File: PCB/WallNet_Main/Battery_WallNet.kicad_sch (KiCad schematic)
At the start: 21 parts, among them J2 USB_C_Receptacle_PowerOnly_6P, J3 Conn_01x04_Pin, U3 BQ25895RTWT

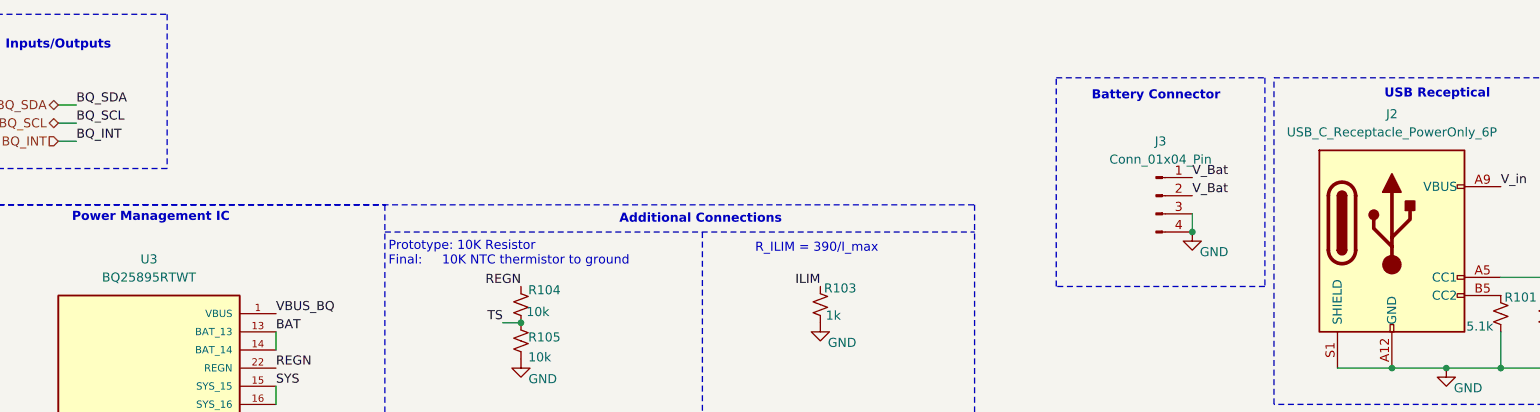
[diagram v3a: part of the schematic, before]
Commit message: Parts complete for schematic
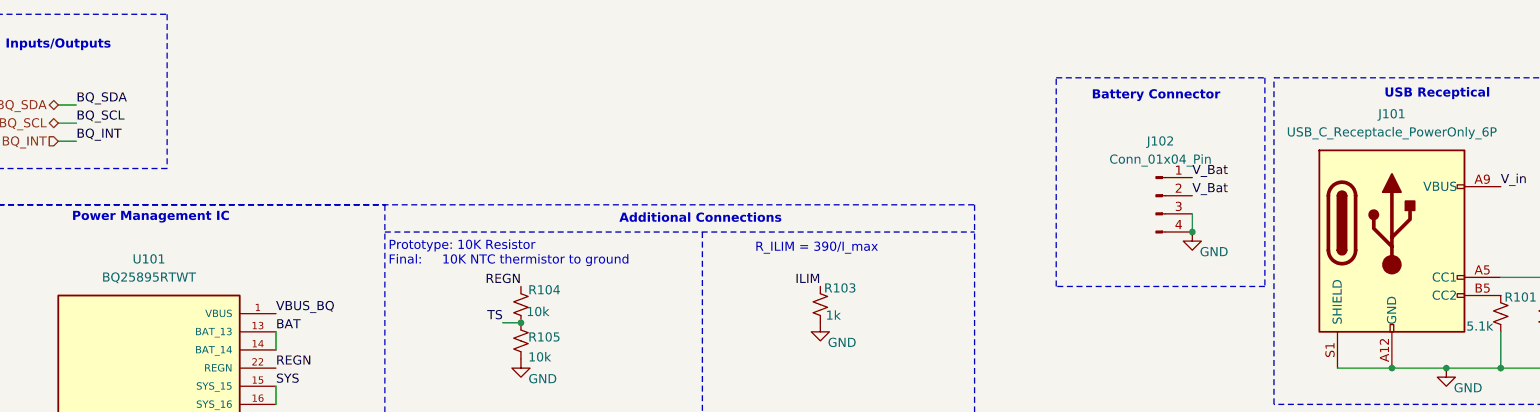
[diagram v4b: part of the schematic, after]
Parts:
- C101, C104, C105, C106, C107: footprint (none) -> Capacitor_SMD:C_0201_0603Metric
- C102, C103: footprint (none) -> Capacitor_SMD:C_0805_2012Metric
- J101: renamed from J2; footprint (none) -> Connector_USB:USB_C_Receptacle_GCT_USB4125-xx-x-0190_6P_TopMnt_Horizontal
- R101, R102, R103, R104, R105, R106, R107, R108, R11: footprint (none) -> Resistor_SMD:R_0201_0603Metric
- renumbered J3 to J102, U3 to U101
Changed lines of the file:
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@@
 			)
 		)
-		(property "Footprint" ""
+		(property "Footprint" "Resistor_SMD:R_0201_0603Metric"
 			(at 119.38 82.55 0)
 			(effects
@@
 		(dnp no)
 		(fields_autoplaced yes)
-		(property "Reference" "J2"
+		(property "Reference" "J101"
 			(at 227.33 27.94 0)
 			(effects
@@
 			)
 		)
-		(property "Footprint" ""
+		(property "Footprint" "Connector_USB:USB_C_Receptacle_GCT_USB4125-xx-x-0190_6P_TopMnt_Horizontal"
 			(at 231.14 43.18 0)
 			(effects
@@
 			(project "WallNet_Main"
 				(path "/3272dd14-9e34-4275-b10b-c06dab1b3ca1/ac25aec4-60b5-4d7f-9f99-a074eef21076"
-					(reference "J2")
+					(reference "J101")
 					(unit 1)
 				)
@@
 			)
 		)
-		(property "Footprint" ""
+		(property "Footprint" "Resistor_SMD:R_0201_0603Metric"
 			(at 248.92 55.88 0)
 			(effects
@@
 			)
 		)
-		(property "Footprint" ""
+		(property "Footprint" "Capacitor_SMD:C_0201_0603Metric"
 			(at 105.41 77.47 0)
 			(effects
@@
 			)
 		)
-		(property "Footprint" ""
+		(property "Footprint" "Capacitor_SMD:C_0201_0603Metric"
 			(at 105.41 121.92 0)
 			(effects
@@
 			)
 		)
-		(property "Footprint" ""
+		(property "Footprint" "Capacitor_SMD:C_0201_0603Metric"
 			(at 123.19 121.92 0)
 			(effects
@@
 		(dnp no)
 		(fields_autoplaced yes)
-		(property "Reference" "U3"
+		(property "Reference" "U101"
 			(at 53.34 48.26 0)
 			(effects
@@
 			(project "WallNet_Main"
 				(path "/3272dd14-9e34-4275-b10b-c06dab1b3ca1/ac25aec4-60b5-4d7f-9f99-a074eef21076"
-					(reference "U3")
+					(reference "U101")
 					(unit 1)
 				)
@@
 			)
 		)
-		(property "Footprint" ""
+		(property "Footprint" "Capacitor_SMD:C_0201_0603Metric"
 			(at 132.08 121.92 0)
 			(effects
@@
 			)
 		)
-		(property "Footprint" ""
+		(property "Footprint" "Resistor_SMD:R_0201_0603Metric"
 			(at 105.41 54.61 0)
 			(effects
@@
 			)
 		)
-		(property "Footprint" ""
+		(property "Footprint" "Resistor_SMD:R_0201_0603Metric"
 			(at 143.51 93.98 0)
 			(effects
@@
 			)
 		)
-		(property "Footprint" ""
+		(property "Footprint" "Resistor_SMD:R_0201_0603Metric"
 			(at 157.48 99.06 0)
 			(effects
@@
 			)
 		)
-		(property "Footprint" ""
+		(property "Footprint" "Capacitor_SMD:C_0201_0603Metric"
 			(at 158.75 77.47 0)
 			(effects
@@
 			)
 		)
-		(property "Footprint" ""
+		(property "Footprint" "Resistor_SMD:R_0201_0603Metric"
 			(at 147.32 54.61 0)
 			(effects
@@
 			)
 		)
-		(property "Footprint" ""
+		(property "Footprint" "Resistor_SMD:R_0201_0603Metric"
 			(at 151.13 96.52 0)
 			(effects
@@
 			)
 		)
-		(property "Footprint" ""
+		(property "Footprint" "Resistor_SMD:R_0201_0603Metric"
 			(at 242.57 55.88 0)
 			(effects
@@
 			)
 		)
-		(property "Footprint" ""
+		(property "Footprint" "Resistor_SMD:R_0201_0603Metric"
 			(at 105.41 59.69 0)
 			(effects
@@
 			)
 		)
-		(property "Footprint" ""
+		(property "Footprint" "Capacitor_SMD:C_0805_2012Metric"
 			(at 93.98 77.47 0)
 			(effects
@@
 			)
 		)
-		(property "Footprint" ""
+		(property "Footprint" "Capacitor_SMD:C_0805_2012Metric"
 			(at 137.16 77.47 0)
 			(effects
@@
 		(dnp no)
 		(fields_autoplaced yes)
-		(property "Reference" "J3"
+		(property "Reference" "J102"
 			(at 194.945 31.75 0)
 			(effects
@@
 			(project "WallNet_Main"
 				(path "/3272dd14-9e34-4275-b10b-c06dab1b3ca1/ac25aec4-60b5-4d7f-9f99-a074eef21076"
-					(reference "J3")
-					(unit 1)
-				)
+					(reference "J102")
+					(unit 1)
+				)

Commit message: Schematic done, updated layout
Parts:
- C101, C104, C105, C106, C107: footprint Capacitor_SMD:C_0201_0603Metric -> Capacitor_SMD:C_0603_1608Metric
- D101: footprint (none) -> Diode_SMD:D_0603_1608Metric
- J102: footprint Connector_Molex:Molex_CLIK-Mate_502494-0470_1x04-1MP_P2.00mm_Horizontal -> Connector_Molex:Molex_PicoBlade_53261-0471_1x04-1MP_P1.25mm_Horizontal
- R101, R102, R103, R104, R105, R106, R107, R108: footprint Resistor_SMD:R_0201_0603Metric -> Resistor_SMD:R_0603_1608Metric
- R109: renamed from R11; footprint Resistor_SMD:R_0201_0603Metric -> Resistor_SMD:R_0603_1608Metric
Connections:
- net VDD_nRF is gone; now on net VDD_nrf: D101.2 (A), R106.1, R107.1, R108.1
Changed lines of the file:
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@@
 	(wire
 		(pts
+			(xy 119.38 73.66) (xy 119.38 74.93)
+		)
+		(stroke
+			(width 0)
+			(type default)
+		)
+	)
+	(wire
+		(pts
 			(xy 40.64 31.75) (xy 43.18 31.75)
 		)
@@
 		)
 	)
-	(label "VDD_nRF"
-		(at 146.05 91.44 180)
-		(effects
-			(font
-				(size 1.27 1.27)
-			)
-			(justify right bottom)
-		)
-	)
 	(label "BTST"
 		(at 71.12 81.28 0)
@@
 		)
 	)
-	(label "VDD_nRF"
-		(at 119.38 74.93 180)
-		(effects
-			(font
-				(size 1.27 1.27)
-			)
-			(justify right bottom)
-		)
-	)
 	(label "CE"
 		(at 113.03 95.25 180)
@@
 	)
 	(global_label "VDD_nrf"
+		(shape input)
+		(at 119.38 73.66 180)
+		(fields_autoplaced yes)
+		(effects
+			(font
+				(size 1.27 1.27)
+			)
+			(justify right)
+		)
+		(property "Intersheetrefs" "${INTERSHEET_REFS}"
+			(at 109.1377 73.66 0)
+			(effects
+				(font
+					(size 1.27 1.27)
+				)
+				(justify right)
+				(hide yes)
+			)
+		)
+	)
+	(global_label "VDD_nrf"
 		(shape output)
 		(at 142.24 119.38 0)
@@
 		)
 	)
+	(global_label "VDD_nrf"
+		(shape input)
+		(at 143.51 91.44 180)
+		(fields_autoplaced yes)
+		(effects
+			(font
+				(size 1.27 1.27)
+			)
+			(justify right)
+		)
+		(property "Intersheetrefs" "${INTERSHEET_REFS}"
+			(at 133.2677 91.44 0)
+			(effects
+				(font
+					(size 1.27 1.27)
+				)
+				(justify right)
+				(hide yes)
+			)
+		)
+	)
 	(hierarchical_label "BQ_INT"
 		(shape input)
@@
 		(on_board yes)
 		(dnp no)
-		(property "Reference" "R11"
+		(property "Reference" "R109"
 			(at 120.396 81.28 0)
 			(effects
@@
 			)
 		)
-		(property "Footprint" "Resistor_SMD:R_0201_0603Metric"
+		(property "Footprint" "Resistor_SMD:R_0603_1608Metric"
 			(at 119.38 82.55 0)
 			(effects
@@
 			(project "WallNet_Main"
 				(path "/3272dd14-9e34-4275-b10b-c06dab1b3ca1/ac25aec4-60b5-4d7f-9f99-a074eef21076"
-					(reference "R11")
+					(reference "R109")
 					(unit 1)
 				)
@@
 			)
 		)
-		(property "Footprint" "Resistor_SMD:R_0201_0603Metric"
+		(property "Footprint" "Resistor_SMD:R_0603_1608Metric"
 			(at 248.92 55.88 0)
 			(effects
@@
 			)
 		)
-		(property "Footprint" "Capacitor_SMD:C_0201_0603Metric"
+		(property "Footprint" "Capacitor_SMD:C_0603_1608Metric"
 			(at 105.41 77.47 0)
 			(effects
@@
 			)
 		)
-		(property "Footprint" "Capacitor_SMD:C_0201_0603Metric"
+		(property "Footprint" "Capacitor_SMD:C_0603_1608Metric"
 			(at 105.41 121.92 0)
 			(effects
@@
 			)
 		)
-		(property "Footprint" "Capacitor_SMD:C_0201_0603Metric"
+		(property "Footprint" "Capacitor_SMD:C_0603_1608Metric"
 			(at 123.19 121.92 0)
 			(effects
@@
 			)
 		)
-		(property "Footprint" "Capacitor_SMD:C_0201_0603Metric"
+		(property "Footprint" "Capacitor_SMD:C_0603_1608Metric"
 			(at 132.08 121.92 0)
 			(effects
@@
 			)
 		)
-		(property "Footprint" "Resistor_SMD:R_0201_0603Metric"
+		(property "Footprint" "Resistor_SMD:R_0603_1608Metric"
 			(at 105.41 54.61 0)
 			(effects
@@
 			)
 		)
-		(property "Footprint" "Resistor_SMD:R_0201_0603Metric"
+		(property "Footprint" "Resistor_SMD:R_0603_1608Metric"
 			(at 143.51 93.98 0)
 			(effects
@@
 			)
 		)
-		(property "Footprint" "Resistor_SMD:R_0201_0603Metric"
+		(property "Footprint" "Resistor_SMD:R_0603_1608Metric"
 			(at 157.48 99.06 0)
 			(effects
@@
 			)
 		)
-		(property "Footprint" "Capacitor_SMD:C_0201_0603Metric"
+		(property "Footprint" "Capacitor_SMD:C_0603_1608Metric"
 			(at 158.75 77.47 0)
 			(effects
@@
 			)
 		)
-		(property "Footprint" "Resistor_SMD:R_0201_0603Metric"
+		(property "Footprint" "Resistor_SMD:R_0603_1608Metric"
 			(at 147.32 54.61 0)
 			(effects
@@
 			)
 		)
-		(property "Footprint" ""
+		(property "Footprint" "Diode_SMD:D_0603_1608Metric"
 			(at 119.38 77.47 90)
 			(effects
@@
 			)
 		)
-		(property "Footprint" "Resistor_SMD:R_0201_0603Metric"
+		(property "Footprint" "Resistor_SMD:R_0603_1608Metric"
 			(at 151.13 96.52 0)
 			(effects
@@
 			)
 		)
-		(property "Footprint" "Resistor_SMD:R_0201_0603Metric"
+		(property "Footprint" "Resistor_SMD:R_0603_1608Metric"
 			(at 242.57 55.88 0)
 			(effects
@@
 			)
 		)
-		(property "Footprint" "Resistor_SMD:R_0201_0603Metric"
+		(property "Footprint" "Resistor_SMD:R_0603_1608Metric"
 			(at 105.41 59.69 0)
 			(effects
@@
 			)
 		)
-		(property "Footprint" "Connector_Molex:Molex_CLIK-Mate_502494-0470_1x04-1MP_P2.00mm_Horizontal"
+		(property "Footprint" "Connector_Molex:Molex_PicoBlade_53261-0471_1x04-1MP_P1.25mm_Horizontal"
 			(at 194.31 39.37 0)
 			(effects

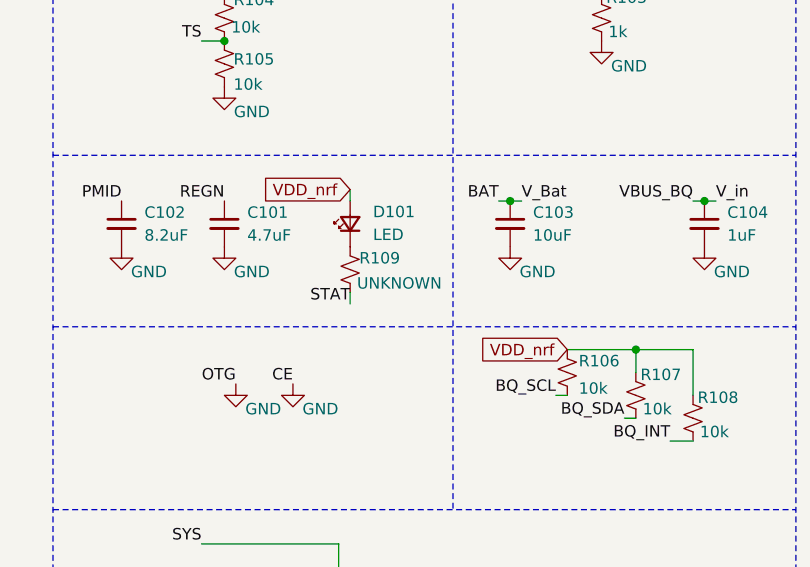
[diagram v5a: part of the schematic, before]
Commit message: added debug LED
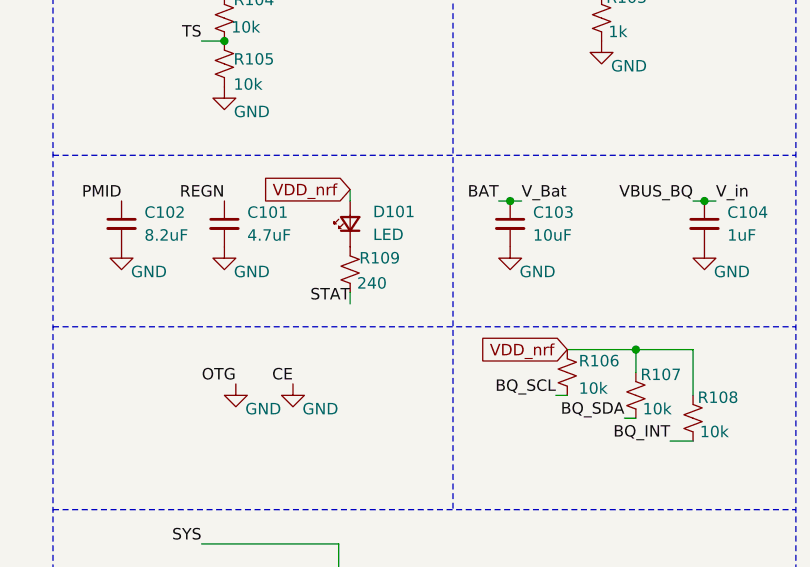
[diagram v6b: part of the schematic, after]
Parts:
- R109: value UNKNOWN -> 240
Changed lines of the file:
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@@
 			)
 		)
-		(property "Value" "UNKNOWN"
+		(property "Value" "240"
 			(at 120.142 84.074 0)
 			(effects

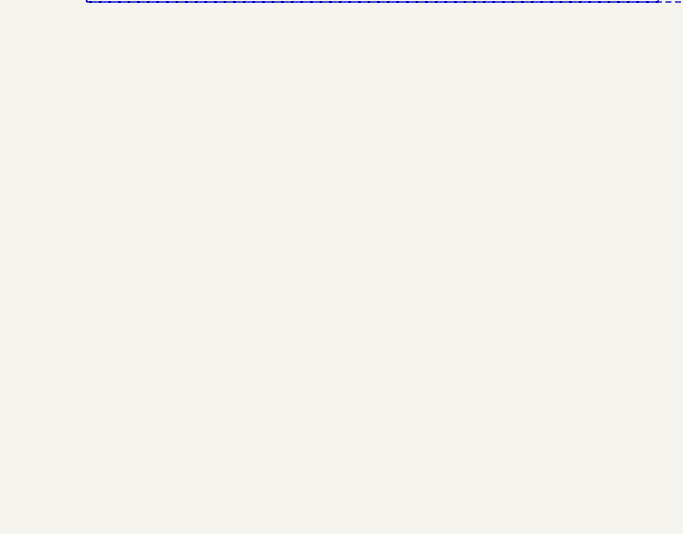
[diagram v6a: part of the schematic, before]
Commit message: "added test point debugging and mounting holes"
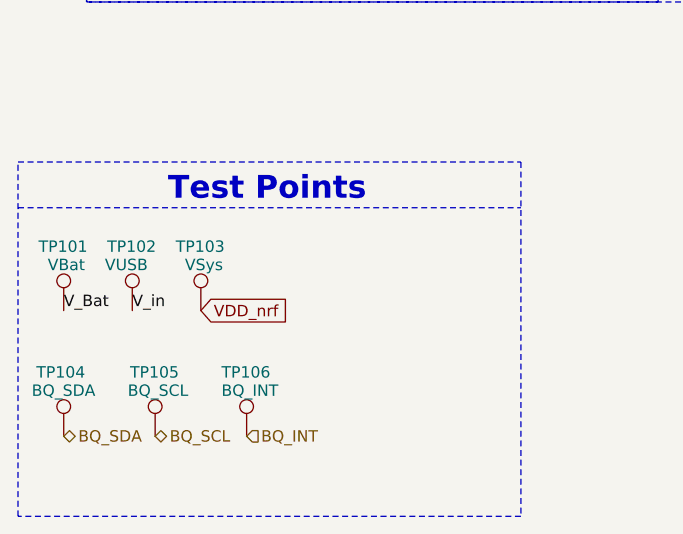
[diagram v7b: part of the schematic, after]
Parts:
- added TP101: VBat, TestPoint:TestPoint_Pad_D1.0mm, symbol Connector:TestPoint
- added TP102: VUSB, TestPoint:TestPoint_Pad_D1.0mm, symbol Connector:TestPoint
- added TP103: VSys, TestPoint:TestPoint_Pad_D1.0mm, symbol Connector:TestPoint
- added TP104: BQ_SDA, 5001:KEYSTONE_5001, symbol Connector:TestPoint
- added TP105: BQ_SCL, 5001:KEYSTONE_5001, symbol Connector:TestPoint
- added TP106: BQ_INT, 5001:KEYSTONE_5001, symbol Connector:TestPoint
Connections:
- net BAT: now also TP101.1
- net BQ_INT: now also TP106.1
- net BQ_SCL: now also TP105.1
- net BQ_SDA: now also TP104.1
- net VBUS_BQ: now also TP102.1
- net VDD_nrf: now also TP103.1
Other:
- note added: "Test Points"

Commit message: Updated, Schematic done, waiting on Layout
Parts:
- L101: footprint (none) -> ISMC:IND_IMSC1008AZER_VIS
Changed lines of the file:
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@@
 			)
 		)
-		(property "Footprint" ""
+		(property "Footprint" "ISMC:IND_IMSC1008AZER_VIS"
 			(at 111.76 119.38 0)
 			(effects
